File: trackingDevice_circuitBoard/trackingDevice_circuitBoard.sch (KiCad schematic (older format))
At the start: 16 parts, among them P1 Digital, P2 COM, P4 Analog, Q1 2N7000, Q2 Q_NPN_EBC, Q3 Q_NPN_EBC, U1 HC-12, U2 GY-NEO6MV2, U3 TP4056

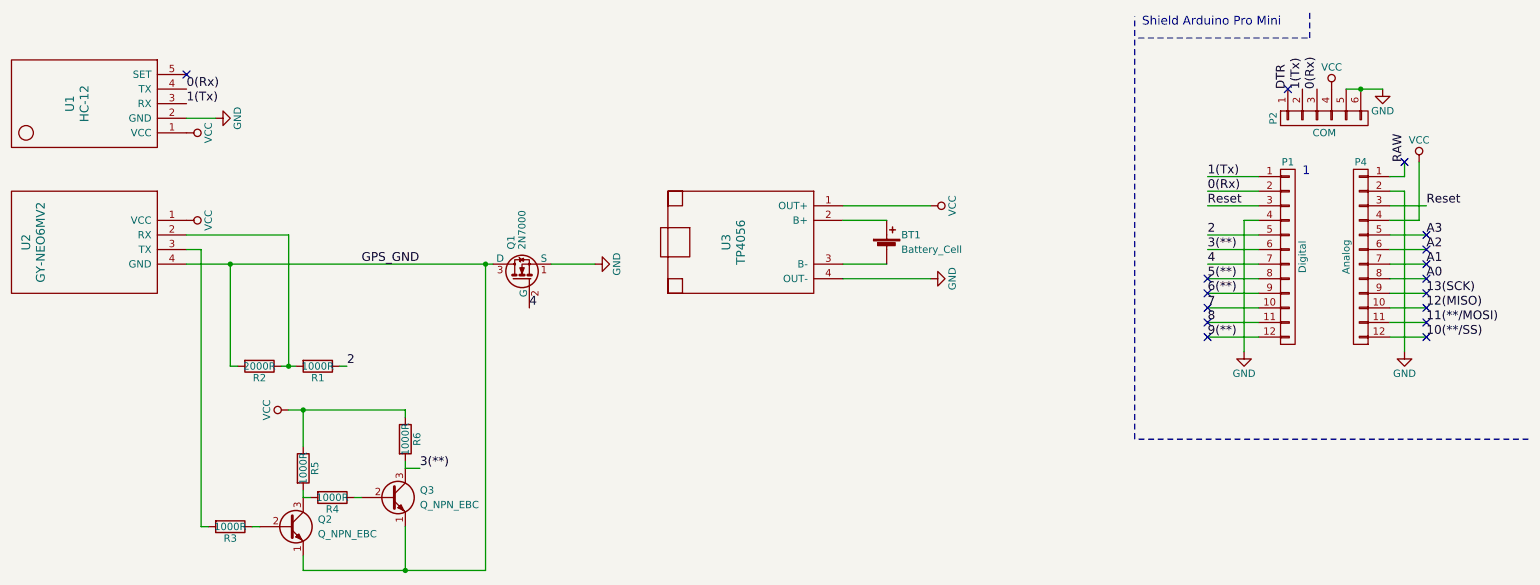
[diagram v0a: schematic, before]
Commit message: Renamed files and folders
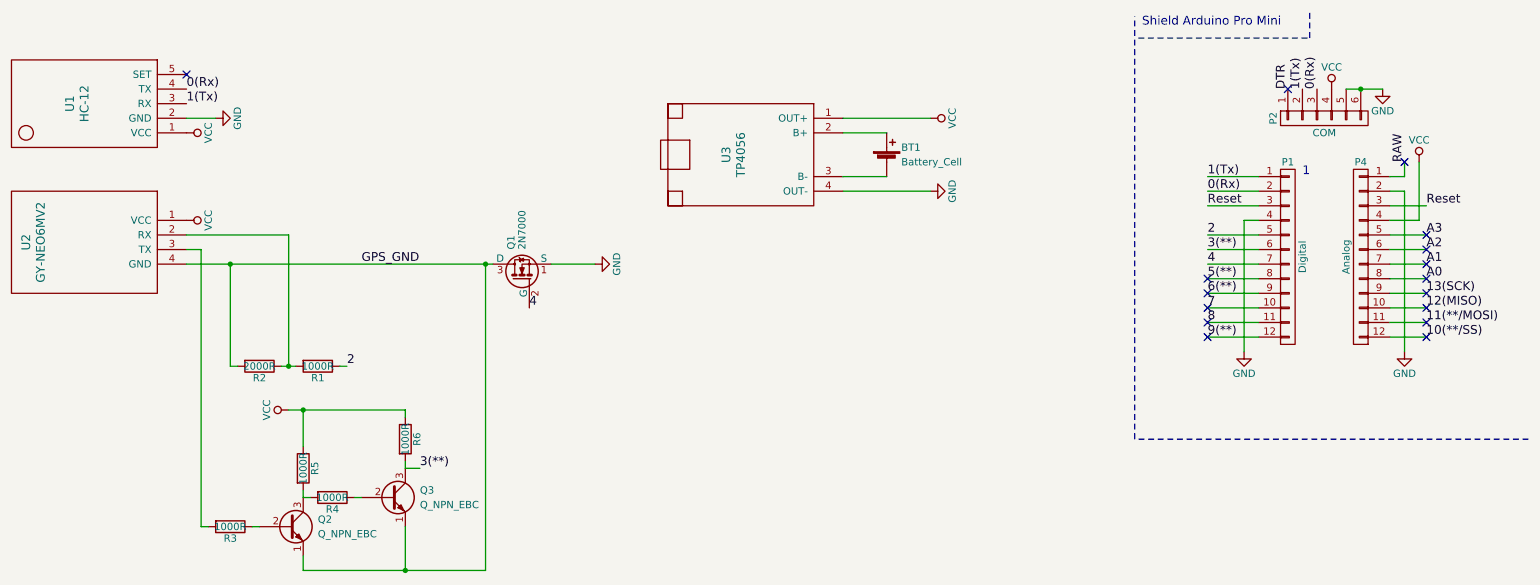
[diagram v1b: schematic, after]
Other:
- moved on the sheet: BT1, U3
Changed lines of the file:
@@
 LIBS:valves
 LIBS:custom_components_library
-LIBS:gpsTracker_trackingDevice_circuitBoard-cache
+LIBS:trackingDevice_circuitBoard-cache
 EELAYER 25 0
 EELAYER END
@@
 L Battery_Cell BT1
 U 1 1 592CB467
-P 6800 2100
-F 0 "BT1" H 6900 2200 50  0000 L CNN
-F 1 "Battery_Cell" H 6900 2100 50  0000 L CNN
-F 2 "Capacitors_THT:CP_Axial_L67.0mm_D23.0mm_P75.00mm_Horizontal" V 6800 2160 50  0001 C CNN
-F 3 "" V 6800 2160 50  0001 C CNN
-	1    6800 2100
+P 6800 1500
+F 0 "BT1" H 6900 1600 50  0000 L CNN
+F 1 "Battery_Cell" H 6900 1500 50  0000 L CNN
+F 2 "Capacitors_THT:CP_Axial_L67.0mm_D23.0mm_P75.00mm_Horizontal" V 6800 1560 50  0001 C CNN
+F 3 "" V 6800 1560 50  0001 C CNN
+	1    6800 1500
 	1    0    0    -1
 $EndComp
@@
 L GND #PWR09
 U 1 1 592CBF25
-P 7100 2300
-F 0 "#PWR09" H 7100 2050 50  0001 C CNN
-F 1 "GND" H 7100 2150 50  0000 C CNN
-F 2 "" H 7100 2300 50  0001 C CNN
-F 3 "" H 7100 2300 50  0001 C CNN
-	1    7100 2300
+P 7100 1700
+F 0 "#PWR09" H 7100 1450 50  0001 C CNN
+F 1 "GND" H 7100 1550 50  0000 C CNN
+F 2 "" H 7100 1700 50  0001 C CNN
+F 3 "" H 7100 1700 50  0001 C CNN
+	1    7100 1700
 	0    -1   -1   0
 $EndComp
@@
 L VCC #PWR010
 U 1 1 592CBF54
-P 7100 1800
-F 0 "#PWR010" H 7100 1650 50  0001 C CNN
-F 1 "VCC" H 7100 1950 50  0000 C CNN
-F 2 "" H 7100 1800 50  0001 C CNN
-F 3 "" H 7100 1800 50  0001 C CNN
-	1    7100 1800
+P 7100 1200
+F 0 "#PWR010" H 7100 1050 50  0001 C CNN
+F 1 "VCC" H 7100 1350 50  0000 C CNN
+F 2 "" H 7100 1200 50  0001 C CNN
+F 3 "" H 7100 1200 50  0001 C CNN
+	1    7100 1200
 	0    1    1    0
 $EndComp
@@
 L TP4056 U3
 U 1 1 592CC948
-P 6100 2000
-F 0 "U3" H 6150 1600 60  0000 C CNN
-F 1 "TP4056" H 6150 1700 60  0000 C CNN
-F 2 "custom_components_library:TP4056_with_protection" H 6100 2000 60  0001 C CNN
-F 3 "" H 6100 2000 60  0001 C CNN
-	1    6100 2000
+P 6100 1400
+F 0 "U3" H 6150 1000 60  0000 C CNN
+F 1 "TP4056" H 6150 1100 60  0000 C CNN
+F 2 "custom_components_library:TP4056_with_protection" H 6100 1400 60  0001 C CNN
+F 3 "" H 6100 1400 60  0001 C CNN
+	1    6100 1400
 	0    1    1    0
 $EndComp
@@
 	4500 2200 4800 2200
 Wire Wire Line
-	6800 2200 6500 2200
-Wire Wire Line
-	6800 1900 6500 1900
-Wire Wire Line
-	6500 1800 7100 1800
-Wire Wire Line
-	6500 2300 7100 2300
+	6800 1600 6500 1600
+Wire Wire Line
+	6800 1300 6500 1300
+Wire Wire Line
+	6500 1200 7100 1200
+Wire Wire Line
+	6500 1700 7100 1700
 Wire Wire Line
 	2000 2100 2100 2100
@@
 Connection ~ 2300 2200
 Wire Wire Line
-	4050 4300 4050 2200
+	4050 2200 4050 4300
 Connection ~ 3500 4300
 Connection ~ 4050 2200

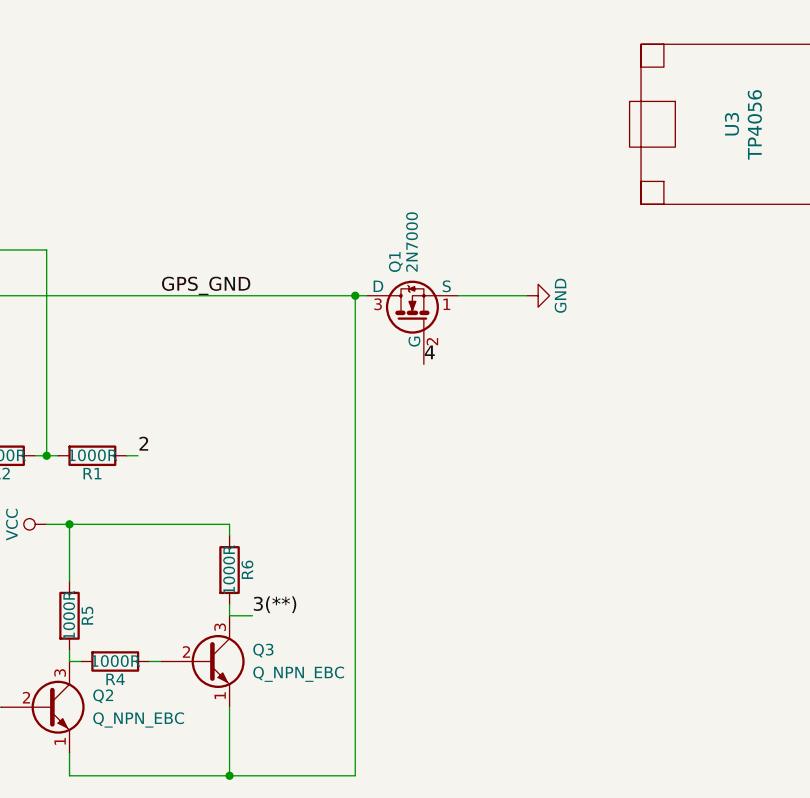
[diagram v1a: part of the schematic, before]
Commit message: Replaced MOSFET with NPN transistor and changed package to TO-126
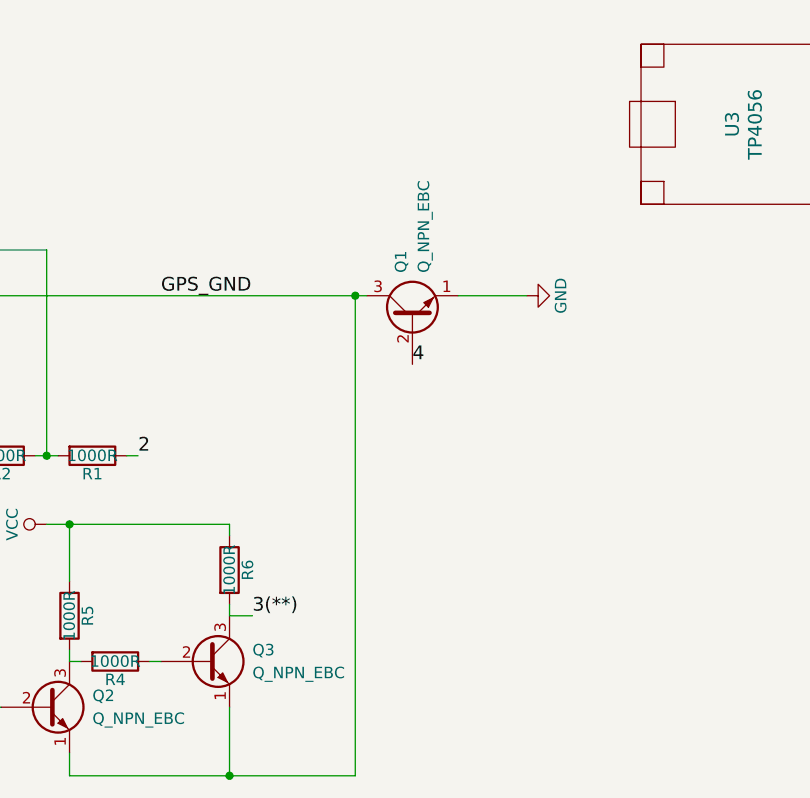
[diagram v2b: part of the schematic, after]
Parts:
- removed Q1: 2N7000, TO_SOT_Packages_THT:TO-92_Inline_Wide, symbol 2N7000
- added Q1: Q_NPN_EBC, TO_SOT_Packages_THT:TO-126_Vertical, symbol Q_NPN_EBC
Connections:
- net 4: now also Q1.2 (B)
- net GND: now also Q1.1 (E)
- net GPS_GND: now also Q1.3 (C)
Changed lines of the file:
@@
 EESchema Schematic File Version 2
+LIBS:trackingDevice_circuitBoard-rescue
 LIBS:power
 LIBS:device
@@
 Text Label 3600 3600 0    60   ~ 0
 3(**)
-Text Label 4350 2500 0    60   ~ 0
+Text Label 4300 2500 0    60   ~ 0
 4
 $Comp
@@
 Wire Wire Line
 	2000 1200 2200 1200
-$Comp
-L 2N7000 Q1
-U 1 1 59346998
-P 4300 2300
-F 0 "Q1" H 4500 2375 50  0000 L CNN
-F 1 "2N7000" H 4500 2300 50  0000 L CNN
-F 2 "TO_SOT_Packages_THT:TO-92_Inline_Wide" H 4500 2225 50  0001 L CIN
-F 3 "" H 4300 2300 50  0001 L CNN
-	1    4300 2300
-	0    -1   -1   0
-$EndComp
 Wire Wire Line
 	2800 4300 4050 4300
@@
 Connection ~ 2300 2200
 Wire Wire Line
-	4050 2200 4050 4300
+	4050 4300 4050 2200
 Connection ~ 3500 4300
 Connection ~ 4050 2200
@@
 Wire Wire Line
 	2000 2200 4100 2200
+$Comp
+L Q_NPN_EBC Q1
+U 1 1 5B1C85F2
+P 4300 2300
+F 0 "Q1" H 4500 2350 50  0000 L CNN
+F 1 "Q_NPN_EBC" H 4500 2250 50  0000 L CNN
+F 2 "TO_SOT_Packages_THT:TO-126_Vertical" H 4500 2400 50  0001 C CNN
+F 3 "" H 4300 2300 50  0001 C CNN
+	1    4300 2300
+	0    -1   -1   0
+$EndComp
 $EndSCHEMATC
